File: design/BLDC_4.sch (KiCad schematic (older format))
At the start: 26 parts, among them K1 SERVO, P1 HALL/Encoder, P101 CANBUS, P3 PWR_COMM, P4 IN+, P5 IN-, P6 MOTOR1, P7 MOTOR2, P9 MOTOR3, X1 MINI-USB-SHIELD-32005-201

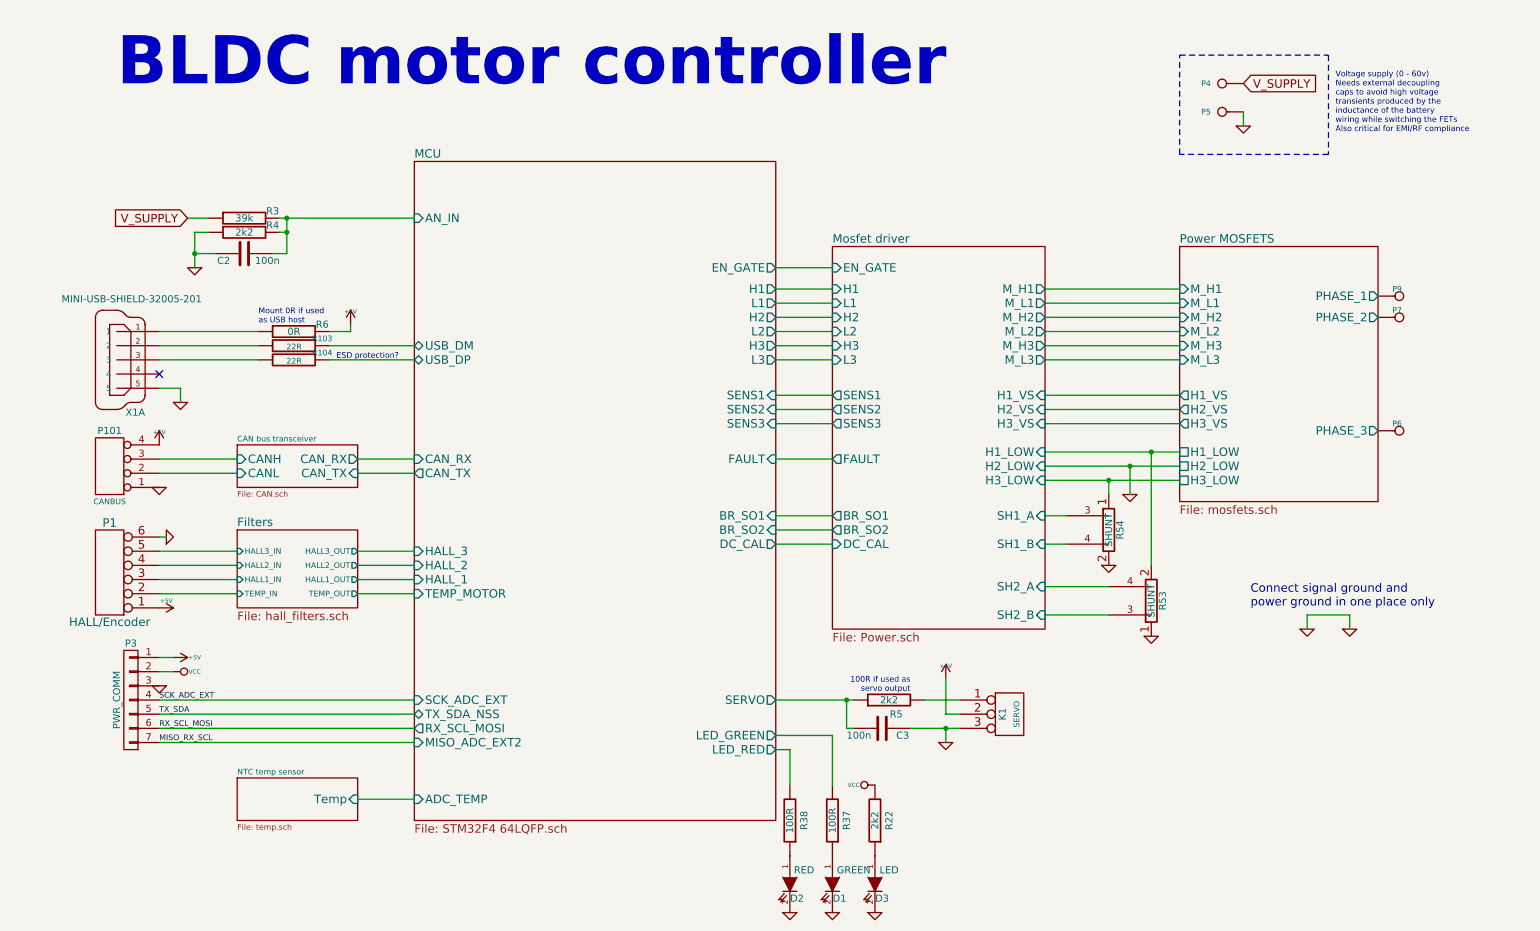
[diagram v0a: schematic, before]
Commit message: Implemented some improvements in schematic, but layout is completely new.
Changes in schematic:
- 3.3V or 5V CAN transceiver can be used
- DRV8301 can also be used and configured via SPI
- JTAG connector changed
- Fixed pinning of P1
- Some additional decoupling and/or filtering of analog signals
- Improved buck design according TI Webench recommendation
- Changed some component values
- maybe others...

Changes in layout:
- completely new layout
- placement of the big components is unchanged
- CAN connector rotated by 180°
- kept one layer free as a good GND plane
- many traces should be shorter and have lower impedance now
- improved buck layout

Other changes:
- updated gerber files
- updated PDFs (schematic and component placement)
- deleted all outdated files except libraries and datasheets
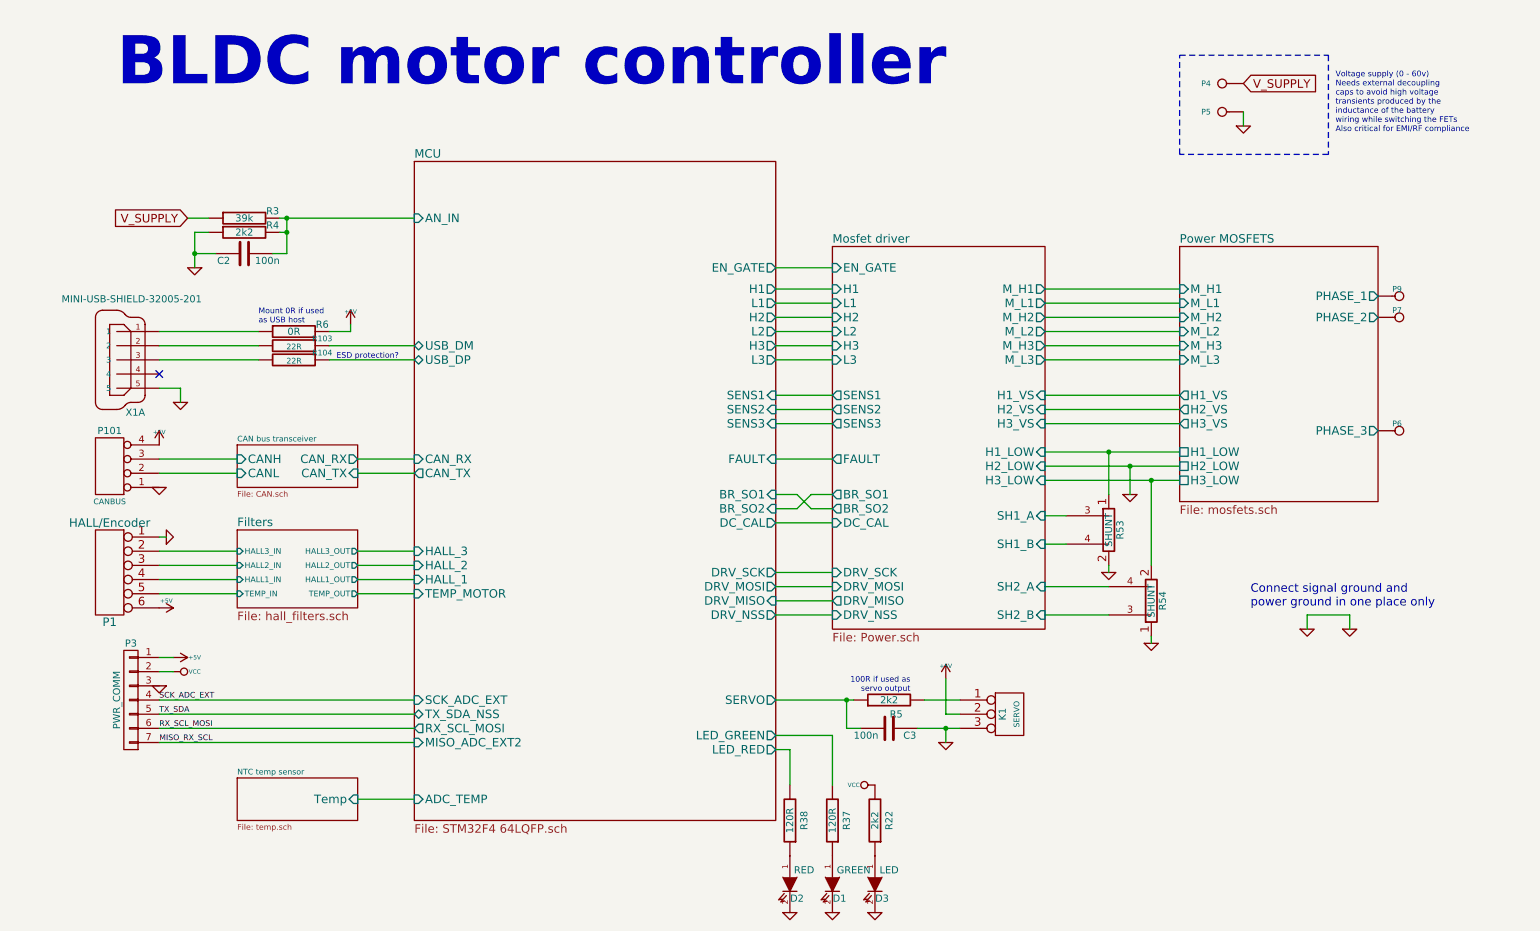
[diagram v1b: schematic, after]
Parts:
- P1: footprint CRF1:MICRO_JST_6 -> pikim:b6b-ph-kl
- P3: footprint CRF1:b7b-ph-kl -> pikim:b7b-ph-kl
- R37, R38: value 100R -> 120R
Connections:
- net +5V: now also P1.6; no longer P1.1
- net Filters/HALL1_IN: now also P1.4; no longer P1.3
- net Filters/HALL2_IN: now also P1.3; no longer P1.4
- net Filters/HALL3_IN: now also P1.2; no longer P1.5
- net Filters/TEMP_IN: now also P1.5; no longer P1.2
- net GND: now also P1.1, R53.2, R54.1; no longer P1.6, R53.1, R54.2
- net Mosfet driver/H1_LOW: now also R53.1; no longer R53.2
- net Mosfet driver/H3_LOW: now also R54.2; no longer R54.1
- net Mosfet driver/SH1_A: now also R53.3; no longer R54.3
- net Mosfet driver/SH1_B: now also R53.4; no longer R54.4
- net Mosfet driver/SH2_A: now also R54.4; no longer R53.4
- net Mosfet driver/SH2_B: now also R54.3; no longer R53.3
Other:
- moved on the sheet: C3, R53, R54
